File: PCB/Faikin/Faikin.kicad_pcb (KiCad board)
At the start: 2 copper layers, 70 x 70 mm, 31 parts, among them J1 1x5, J2 TC2030-USB-NL, J3 Reset, Q1 BSS138PS, U3 MD8942, U4 ESP32-S3-MINI-1

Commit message: New PCB
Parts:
- removed C10: 100nF, RevK:C_0603_
- removed C8: 10uF 35V, RevK:C_0603_
- removed C9: 10uF 6.3V, RevK:C_0603_
- removed L2: 10uH, RevK:L_4x4_
- removed R10: 39k2, RevK:R_0402_
- removed R11: 1M, RevK:R_0402_
- removed R9: 124k, RevK:R_0402_
- removed U3: MD8942, RevK:SOT-23-6-MD8942
- added C1: 100nF, RevK:C_0201, F.Cu at (138.0, 64.6)
- added C15: 47uF 6V, RevK:C_0805, F.Cu at (143.6, 62.2)
- added C16: 100nF 25V, RevK:C_0402, F.Cu at (138.1, 68.5)
- added C17: 22uF 25V, RevK:C_0805, F.Cu at (143.6, 66.0)
- added C18: 100nF, RevK:C_0201, F.Cu at (140.4, 64.6)
- added C19: 18pF, RevK:C_0201, F.Cu at (139.2, 64.6)
- added C3: 100nF 25V, RevK:C_0402, F.Cu at (144.3, 68.7)
- added C4: 100nF, RevK:C_0201, F.Cu at (144.2, 70.7)
- added C7: 100nF, RevK:C_0201, F.Cu at (142.1, 64.9)
- added L1: 4.7uH, RevK:L_5x5, F.Cu at (141.2, 70.2)
- added R5: 100k, RevK:R_0201, F.Cu at (139.8, 64.6)
- added R6: 150k 1%, RevK:R_0201, F.Cu at (138.6, 64.6)
- added R8: 33k 1%, RevK:R_0201, F.Cu at (138.3, 65.6)
- added TP2: TestPoint, RevK:PAD-2mm, B.Cu at (133.0, 69.8)
- added TP3: TestPoint, RevK:PAD-2mm, B.Cu at (130.7, 69.8)
- added TP4: TestPoint, RevK:PAD-2mm, B.Cu at (128.5, 69.8)
- added TP5: TestPoint, RevK:PAD-2mm, B.Cu at (126.2, 69.8)
- added TP6: TestPoint, RevK:PAD-2mm, B.Cu at (126.2, 60.0)
- added U1: TPS562246, RevK:SOT-563, F.Cu at (139.7, 66.4)
- C2, C6: footprint RevK:C_0402 -> RevK:C_0201
- C5: value 22uF -> 100nF; footprint RevK:C_0603 -> RevK:C_0201
- R1, R2, R3: footprint RevK:R_0402 -> RevK:R_0201
- moved C2 10.8 mm to (138.1, 72.1), turned to -90 degrees
- moved C5 2.42 mm to (143.6, 64.1), turned to 180 degrees
- moved TP1 1.03 mm to (141.5, 62.2)
- moved D1 0.94 mm to (139.8, 62.2)
- moved C6 0.32 mm to (138.6, 58.3)
- moved R1 0.20 mm to (143.5, 59.8)
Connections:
- net Net-(U4-EN) renamed RST
- C2 pad 1: +3.3V -> GND
- C2 pad 2: GND -> +3.3V
- C5 pad 1: +3.3V -> GND
- C5 pad 2: GND -> +3.3V
- U4 pad 19: +3.3V -> GND
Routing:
- net +3.3V: track 31.9 -> 61.9 mm, vias 2 -> 6
- net DC: track 12.3 -> 36.9 mm, vias 1 -> 3
- net SW: track 0.00 -> 9.77 mm, vias 0 -> 2
- net GND: track 4.05 -> 13.6 mm, vias 52 -> 54
- net D+: track 39.6 -> 42.1 mm
- net FB: track 0.00 -> 1.97 mm
- net RST: track 17.2 -> 19.0 mm
- net Net-(J1-Pin_3): track 43.6 -> 42.5 mm
- net BST: track 0.00 -> 0.86 mm
- net LED: track 1.83 -> 2.64 mm
- net EN: track 0.00 -> 0.66 mm
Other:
- board text added: "3V3"
- board text added: "D+"
- board text added: "D-"
- board text added: "EN"
- board text removed: "5060634238151"

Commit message: Library update
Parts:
- added TP7: TestPoint, RevK:PAD-2mm, B.Cu at (135.2, 69.8)
- moved C6 0.67 mm to (138.0, 58.0), turned to -90 degrees
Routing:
- net DC: track 36.9 -> 38.6 mm
- net +3.3V: track 61.9 -> 60.4 mm
- net D-: track 35.6 -> 34.6 mm
- net GND: track 13.6 -> 14.6 mm, vias 54 -> 52
- net RST: track 19.0 -> 19.7 mm
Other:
- board text added: "DC"

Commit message: Layout
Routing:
- net D-: track 34.6 -> 40.3 mm
- net D+: track 42.0 -> 44.6 mm

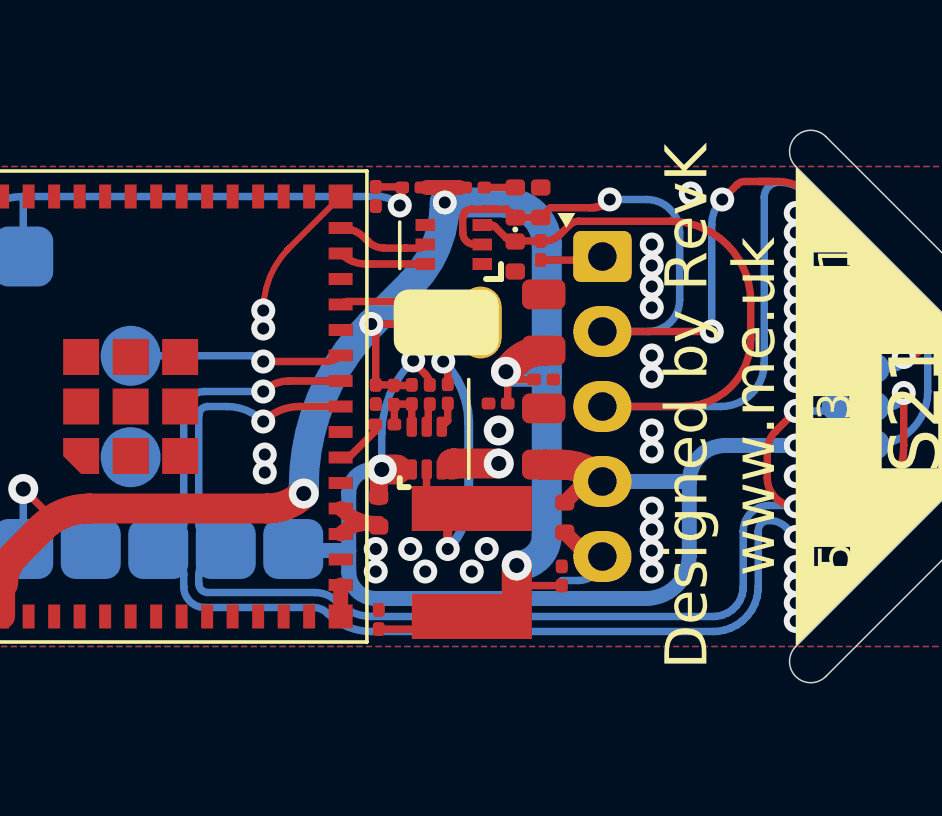
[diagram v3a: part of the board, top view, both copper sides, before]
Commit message: New 0201 footprint
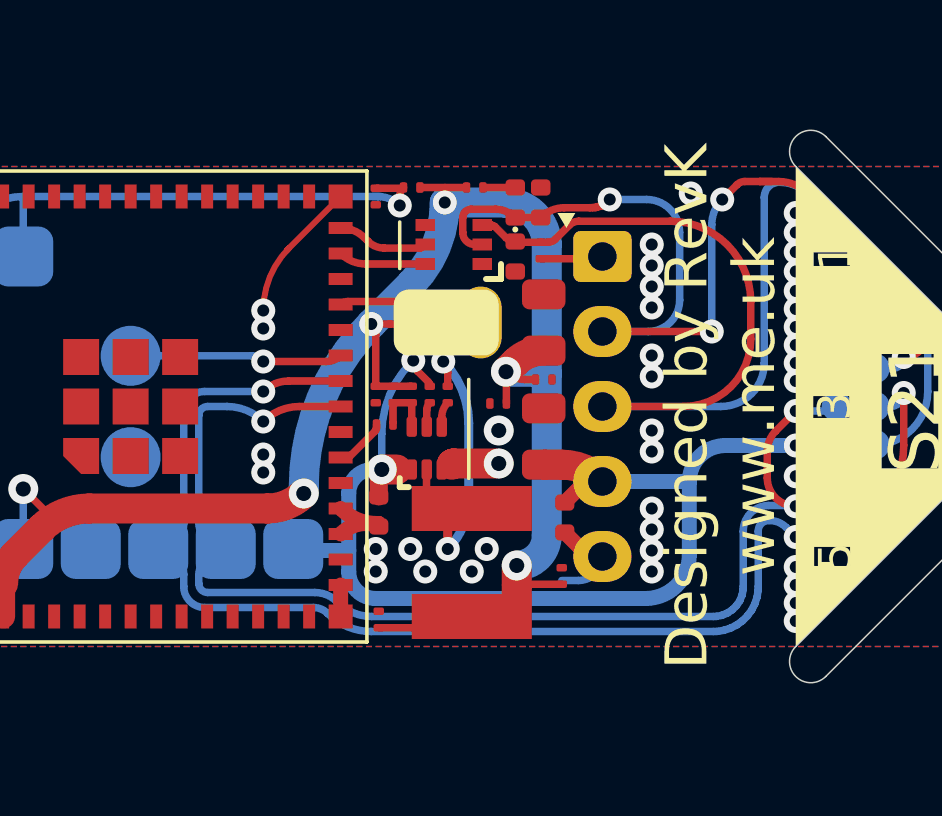
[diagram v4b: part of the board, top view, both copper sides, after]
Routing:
- net +3.3V: track 60.4 -> 59.5 mm

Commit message: Library update
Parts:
- R5: value 100k -> 150k 1%
- turned R5 to 90 degrees
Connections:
- R5 pad 1: DC -> EN
- R5 pad 2: EN -> DC

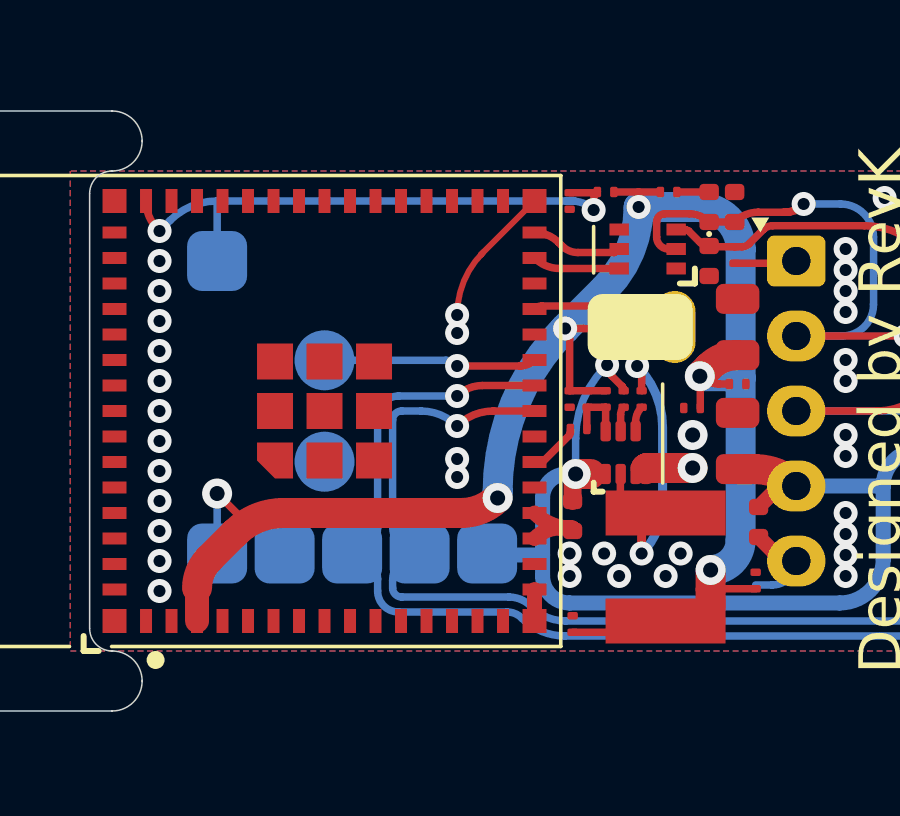
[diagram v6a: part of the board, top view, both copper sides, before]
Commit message: Revised test points
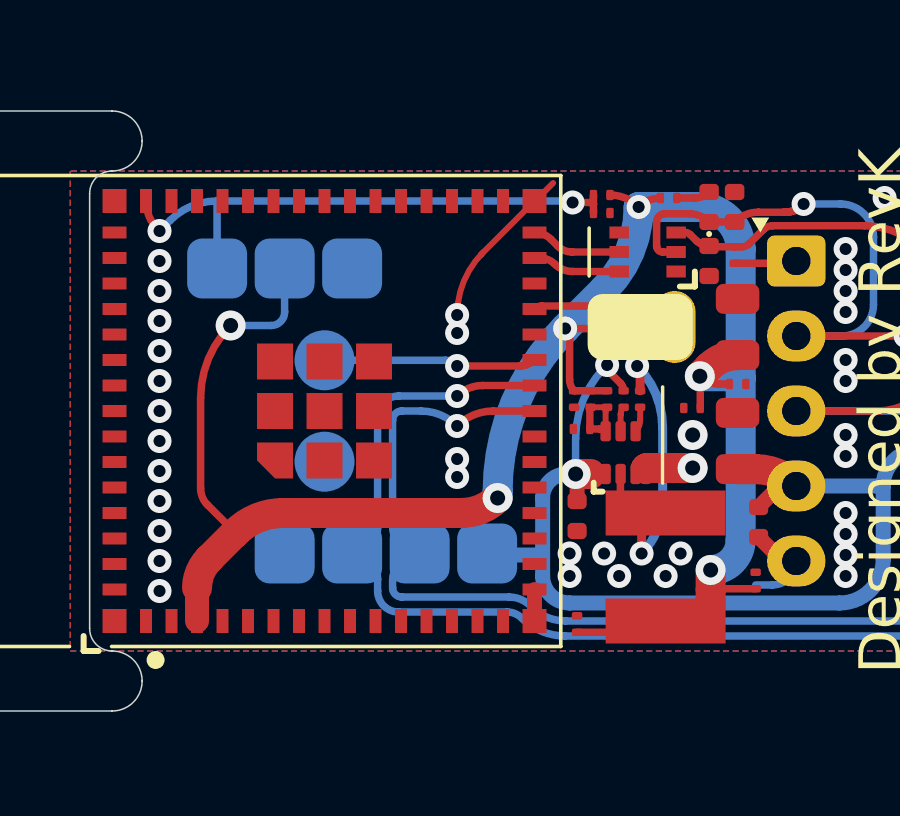
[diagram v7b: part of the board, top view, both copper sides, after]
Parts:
- added TP8: TestPoint, RevK:PAD-2mm, B.Cu at (130.8, 60.2)
- moved TP5 9.76 mm to (128.5, 60.2)
- moved C6 1.14 mm to (139.1, 58.4), turned to 0 degrees
- moved TP6 0.25 mm to (126.2, 60.2)
- moved R2 0.20 mm to (141.3, 57.9)
- moved R3 0.16 mm to (139.1, 57.8)
- moved C1 0.15 mm to (138.2, 64.6)
- moved C16 0.15 mm to (138.2, 68.5)
- moved C2 0.15 mm to (138.2, 72.1)
- moved Q1 0.10 mm to (140.6, 59.7)
- moved R6 0.10 mm to (138.7, 64.6)
- moved R8 0.10 mm to (138.4, 65.6)
- moved C18 0.05 mm to (140.3, 64.6)
- moved C19 0.05 mm to (139.2, 64.6)
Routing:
- net +3.3V: track 59.5 -> 66.4 mm
- net GND: track 14.6 -> 11.2 mm
- net RST: track 19.8 -> 18.8 mm
- net FB: track 2.13 -> 2.64 mm
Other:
- board text removed: "DC"

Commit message: Library update
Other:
- board text added: "+"
- board text added: "-"
- board text removed: "TC2030"
